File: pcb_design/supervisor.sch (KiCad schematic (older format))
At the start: 27 parts

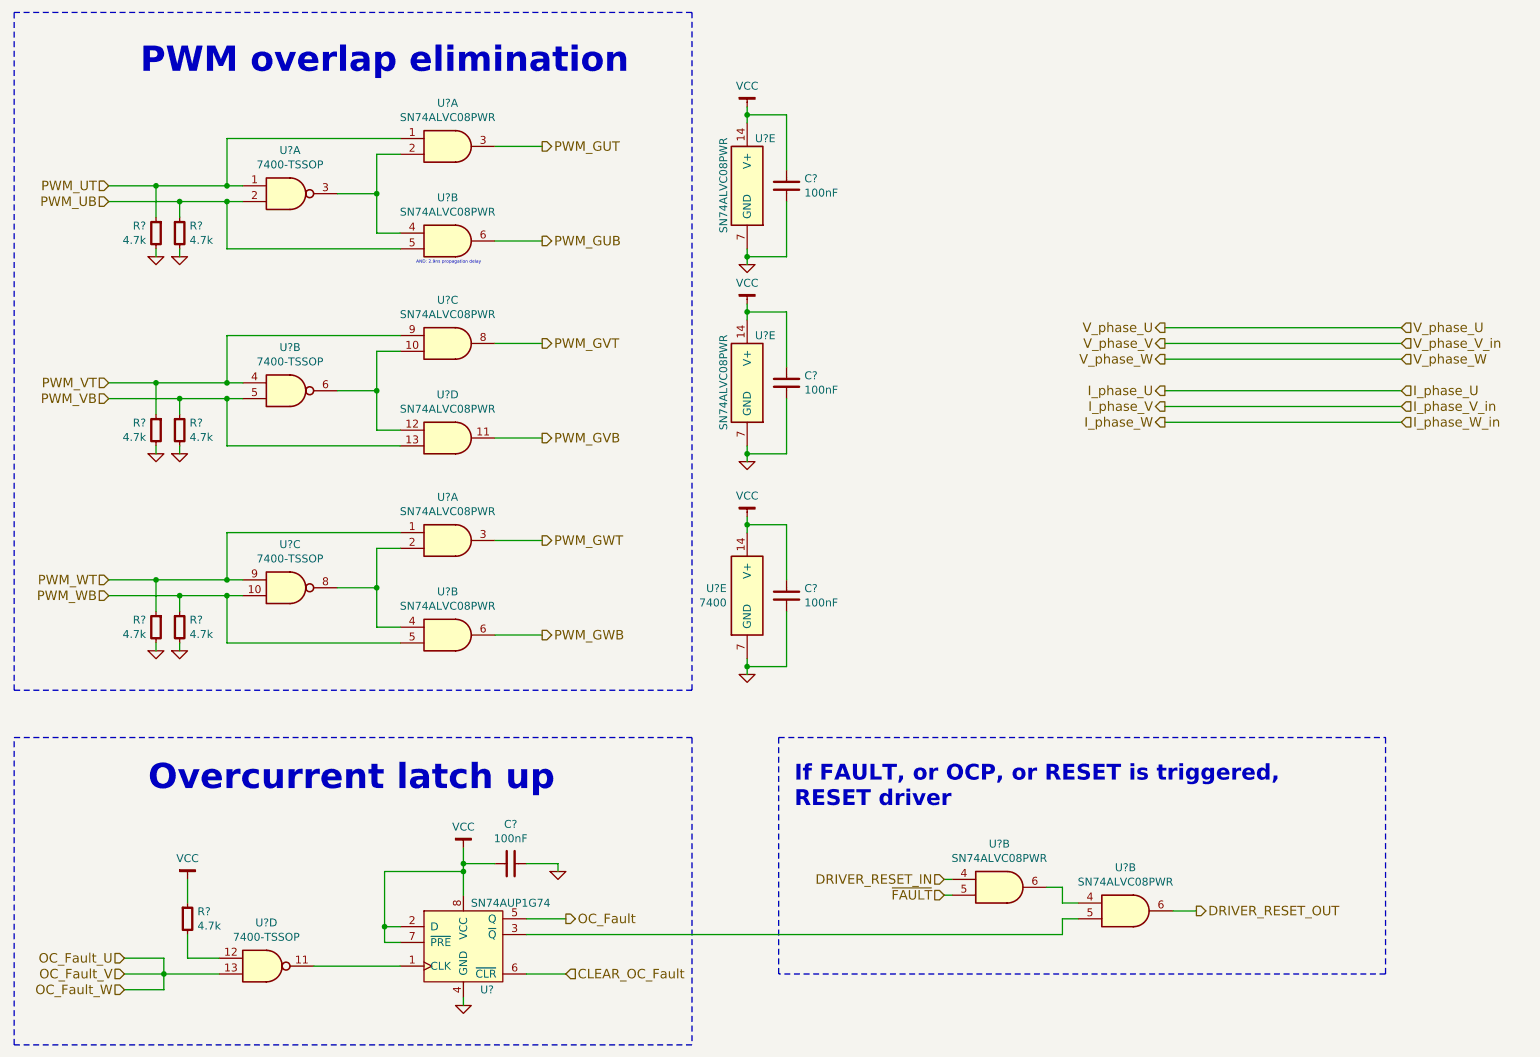
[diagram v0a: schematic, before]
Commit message: Updated MCU sheet to comply with VESC 6 pinout. Added 5v analog inputs and updated some labels
Signed-off-by: Marcos Chaparro <mchaparro@paltatech.com>
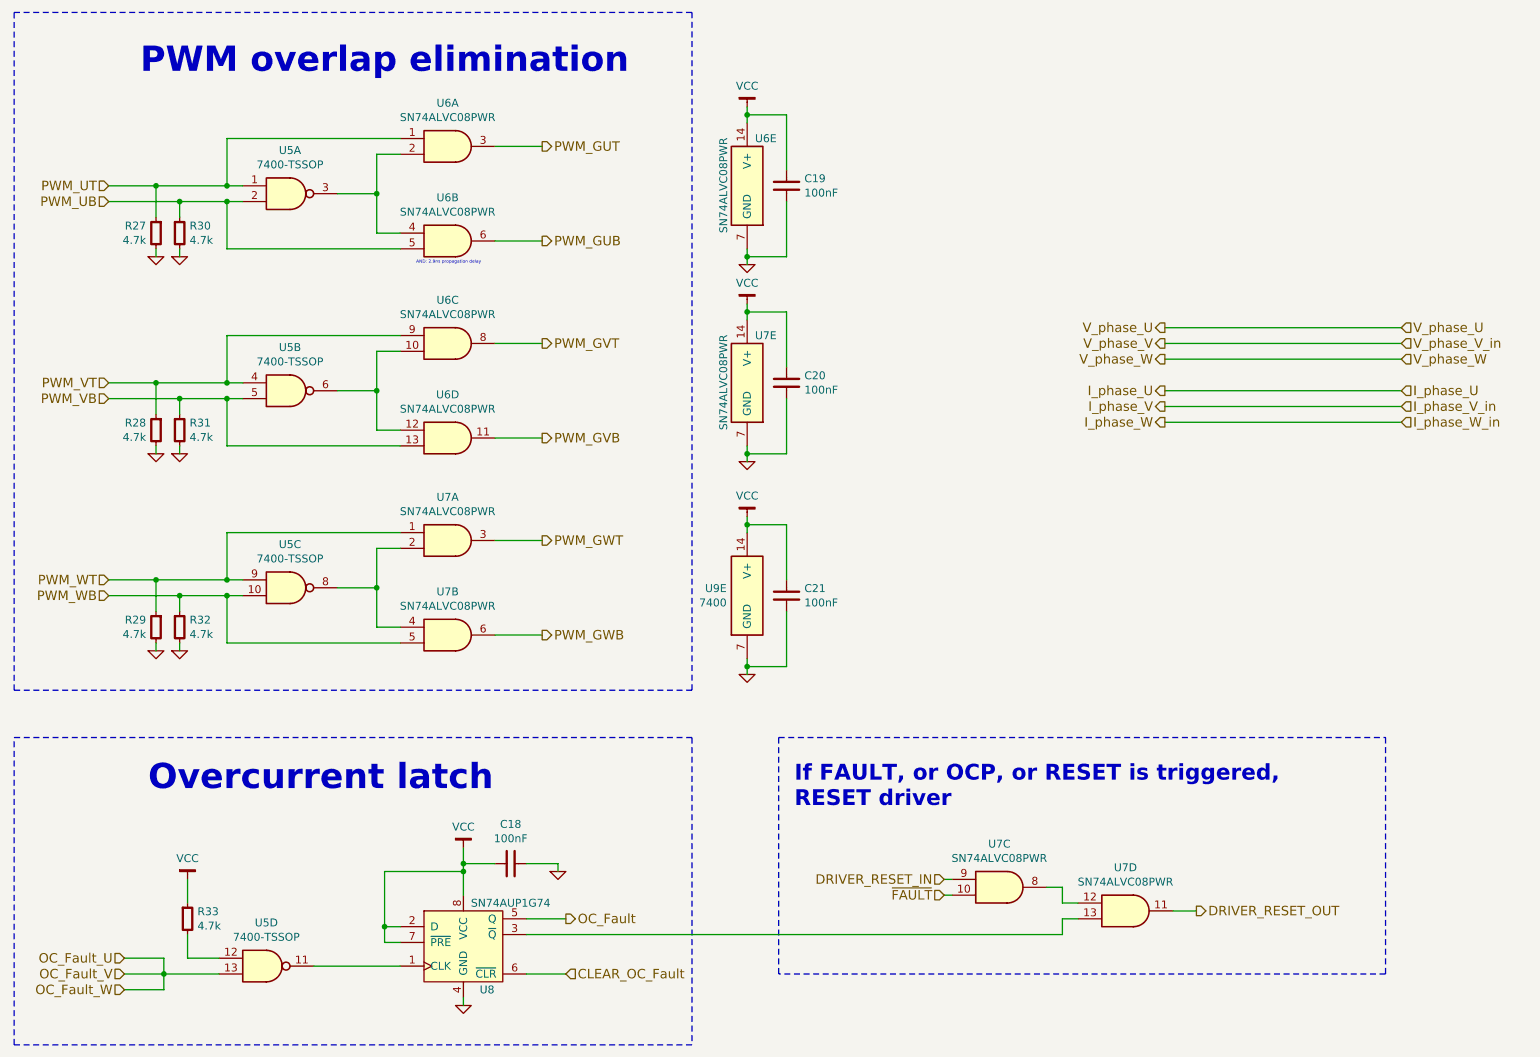
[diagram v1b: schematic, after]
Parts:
- gave numbers to parts that had none: 16
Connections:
- net DRIVER_RESET_IN: now also U7.9 (D1C); no longer U7.4 (D1B)
- net DRIVER_RESET_OUT: now also U7.11 (QD); no longer U7.6 (QB)
- net ~FAULT: now also U7.10 (D2C); no longer U7.5 (D2B)
- net at U8.3 (~Q): now also U7.13 (D2D); no longer U7.5 (D2B)
- new net: U7.12 (D1D), U7.8 (QC)
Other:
- note added: "Overcurrent latch"
- note removed: "Overcurrent latch up"

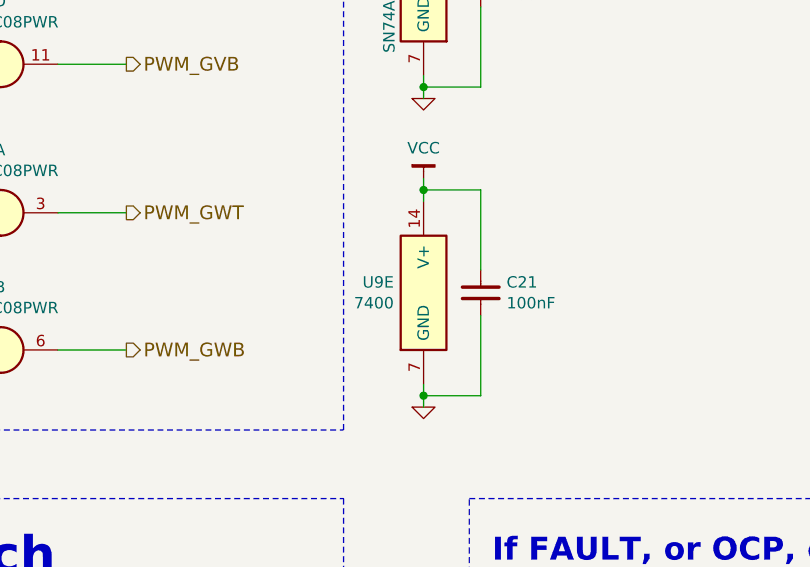
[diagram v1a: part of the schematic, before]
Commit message: Components placement, 3D models, updated some footprints to nominal IPC type
Signed-off-by: Marcos Chaparro <mchaparro@paltatech.com>
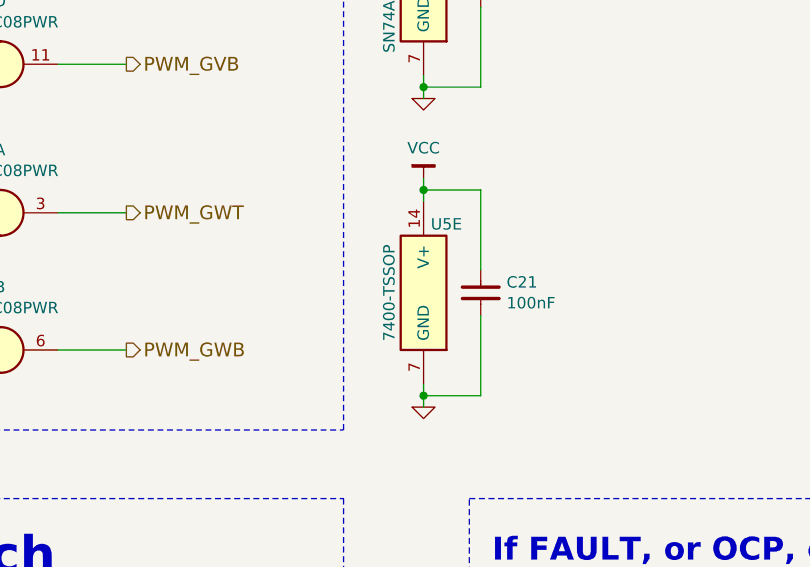
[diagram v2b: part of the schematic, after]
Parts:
- removed U9: 7400, symbol 7400
- added unit 5 of U5
- U8: footprint (none) -> IPC7351-Nominal:SOP50P310X100-8
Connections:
- net GND: now also U5.7 (GND)
- net VCC: now also U5.14 (V+)
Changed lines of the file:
@@
 $Descr A4 11693 8268
 encoding utf-8
-Sheet 8 12
+Sheet 7 12
 Title ""
 Date ""
@@
 Connection ~ 2000 2050
 $Comp
-L GND #PWR056
+L GND #PWR44
 U 1 1 588831C2
 P 1850 2400
-F 0 "#PWR056" H 1850 2400 30  0001 C CNN
+F 0 "#PWR44" H 1850 2400 30  0001 C CNN
 F 1 "GND" H 1850 2330 30  0001 C CNN
 F 2 "" H 1850 2400 60  0000 C CNN
@@
 	1850 2400 1850 2350
 $Comp
-L GND #PWR057
+L GND #PWR47
 U 1 1 58883201
 P 2000 2400
-F 0 "#PWR057" H 2000 2400 30  0001 C CNN
+F 0 "#PWR47" H 2000 2400 30  0001 C CNN
 F 1 "GND" H 2000 2330 30  0001 C CNN
 F 2 "" H 2000 2400 60  0000 C CNN
@@
 	1    2700 2000
 	1    0    0    -1
-$EndComp
-$Comp
-L 7400 U9
-U 5 1 588843C8
-P 5600 4150
-F 0 "U9" H 5730 3796 50  0000 L CNN
-F 1 "7400" H 5730 3705 50  0000 L CNN
-F 2 "" H 5600 3250 50  0001 C CNN
-F 3 "http://www.nxp.com/documents/data_sheet/74HC_HCT00.pdf" H 5600 3150 50  0001 C CNN
-	5    5600 4150
-	-1   0    0    -1
 $EndComp
 $Comp
@@
 Connection ~ 2000 3300
 $Comp
-L GND #PWR058
+L GND #PWR45
 U 1 1 588824FD
 P 1850 3650
-F 0 "#PWR058" H 1850 3650 30  0001 C CNN
+F 0 "#PWR45" H 1850 3650 30  0001 C CNN
 F 1 "GND" H 1850 3580 30  0001 C CNN
 F 2 "" H 1850 3650 60  0000 C CNN
@@
 	1850 3650 1850 3600
 $Comp
-L GND #PWR059
+L GND #PWR48
 U 1 1 58882504
 P 2000 3650
-F 0 "#PWR059" H 2000 3650 30  0001 C CNN
+F 0 "#PWR48" H 2000 3650 30  0001 C CNN
 F 1 "GND" H 2000 3580 30  0001 C CNN
 F 2 "" H 2000 3650 60  0000 C CNN
@@
 Connection ~ 2000 4550
 $Comp
-L GND #PWR060
+L GND #PWR46
 U 1 1 5888288C
 P 1850 4900
-F 0 "#PWR060" H 1850 4900 30  0001 C CNN
+F 0 "#PWR46" H 1850 4900 30  0001 C CNN
 F 1 "GND" H 1850 4830 30  0001 C CNN
 F 2 "" H 1850 4900 60  0000 C CNN
@@
 	1850 4900 1850 4850
 $Comp
-L GND #PWR061
+L GND #PWR49
 U 1 1 58882893
 P 2000 4900
-F 0 "#PWR061" H 2000 4900 30  0001 C CNN
+F 0 "#PWR49" H 2000 4900 30  0001 C CNN
 F 1 "GND" H 2000 4830 30  0001 C CNN
 F 2 "" H 2000 4900 60  0000 C CNN
@@
 F 0 "U8" H 3950 6550 50  0000 C CNN
 F 1 "SN74AUP1G74" H 4100 7100 50  0000 C CNN
-F 2 "" H 3800 6800 20  0001 C CNN
+F 2 "IPC7351-Nominal:SOP50P310X100-8" H 3800 6800 20  0001 C CNN
 F 3 "" H 3800 6800 20  0001 C CNN
 	1    3800 6800
@@
 $EndComp
 $Comp
-L GND #PWR062
+L GND #PWR52
 U 1 1 5888A11E
 P 3800 7150
-F 0 "#PWR062" H 3800 7150 30  0001 C CNN
+F 0 "#PWR52" H 3800 7150 30  0001 C CNN
 F 1 "GND" H 3800 7080 30  0001 C CNN
 F 2 "" H 3800 7150 60  0000 C CNN
@@
 	4400 6250 4400 6300
 $Comp
-L GND #PWR063
+L GND #PWR53
 U 1 1 5888A46C
 P 4400 6300
-F 0 "#PWR063" H 4400 6300 30  0001 C CNN
+F 0 "#PWR53" H 4400 6300 30  0001 C CNN
 F 1 "GND" H 4400 6230 30  0001 C CNN
 F 2 "" H 4400 6300 60  0000 C CNN
@@
 AR Path="/5886DA84/588980B5" Ref="#PWR?"  Part="1"
 AR Path="/588C2790/588980B5" Ref="#PWR?"  Part="1"
-AR Path="/5888D059/588980B5" Ref="#PWR064"  Part="1"
-F 0 "#PWR064" H 3800 6200 30  0001 C CNN
+AR Path="/5888D059/588980B5" Ref="#PWR51"  Part="1"
+F 0 "#PWR51" H 3800 6200 30  0001 C CNN
 F 1 "VCC" H 3800 6283 50  0000 C CNN
 F 2 "" H 3800 6150 60  0000 C CNN
@@
 AR Path="/5886DA84/58898103" Ref="#PWR?"  Part="1"
 AR Path="/588C2790/58898103" Ref="#PWR?"  Part="1"
-AR Path="/5888D059/58898103" Ref="#PWR065"  Part="1"
-F 0 "#PWR065" H 2050 6400 30  0001 C CNN
+AR Path="/5888D059/58898103" Ref="#PWR50"  Part="1"
+F 0 "#PWR50" H 2050 6400 30  0001 C CNN
 F 1 "VCC" H 2050 6483 50  0000 C CNN
 F 2 "" H 2050 6350 60  0000 C CNN
@@
 AR Path="/5886DA84/588981CE" Ref="#PWR?"  Part="1"
 AR Path="/588C2790/588981CE" Ref="#PWR?"  Part="1"
-AR Path="/5888D059/588981CE" Ref="#PWR066"  Part="1"
-F 0 "#PWR066" H 5600 4100 30  0001 C CNN
+AR Path="/5888D059/588981CE" Ref="#PWR58"  Part="1"
+F 0 "#PWR58" H 5600 4100 30  0001 C CNN
 F 1 "VCC" H 5600 4183 50  0000 C CNN
 F 2 "" H 5600 4050 60  0000 C CNN
@@
 AR Path="/5886DA84/58898412" Ref="#PWR?"  Part="1"
 AR Path="/588C2790/58898412" Ref="#PWR?"  Part="1"
-AR Path="/5888D059/58898412" Ref="#PWR067"  Part="1"
-F 0 "#PWR067" H 5600 1500 30  0001 C CNN
+AR Path="/5888D059/58898412" Ref="#PWR54"  Part="1"
+F 0 "#PWR54" H 5600 1500 30  0001 C CNN
 F 1 "VCC" H 5600 1583 50  0000 C CNN
 F 2 "" H 5600 1450 60  0000 C CNN
@@
 AR Path="/5886DA84/588984F1" Ref="#PWR?"  Part="1"
 AR Path="/588C2790/588984F1" Ref="#PWR?"  Part="1"
-AR Path="/5888D059/588984F1" Ref="#PWR068"  Part="1"
-F 0 "#PWR068" H 5600 2750 30  0001 C CNN
+AR Path="/5888D059/588984F1" Ref="#PWR56"  Part="1"
+F 0 "#PWR56" H 5600 2750 30  0001 C CNN
 F 1 "VCC" H 5600 2833 50  0000 C CNN
 F 2 "" H 5600 2700 60  0000 C CNN
@@
 	5600 4950 5600 5050
 $Comp
-L GND #PWR069
+L GND #PWR59
 U 1 1 58899228
 P 5600 5050
-F 0 "#PWR069" H 5600 5050 30  0001 C CNN
+F 0 "#PWR59" H 5600 5050 30  0001 C CNN
 F 1 "GND" H 5600 4980 30  0001 C CNN
 F 2 "" H 5600 5050 60  0000 C CNN
@@
 Connection ~ 5600 5000
 $Comp
-L GND #PWR070
+L GND #PWR57
 U 1 1 5889937C
 P 5600 3700
-F 0 "#PWR070" H 5600 3700 30  0001 C CNN
+F 0 "#PWR57" H 5600 3700 30  0001 C CNN
 F 1 "GND" H 5600 3630 30  0001 C CNN
 F 2 "" H 5600 3700 60  0000 C CNN
@@
 $EndComp
 $Comp
-L GND #PWR071
+L GND #PWR55
 U 1 1 588993D2
 P 5600 2450
-F 0 "#PWR071" H 5600 2450 30  0001 C CNN
+F 0 "#PWR55" H 5600 2450 30  0001 C CNN
 F 1 "GND" H 5600 2380 30  0001 C CNN
 F 2 "" H 5600 2450 60  0000 C CNN
@@
 	5850 1500 5600 1500
 Connection ~ 5600 1500
+$Comp
+L 7400 U5
+U 5 1 588A2A9D
+P 5600 4150
+F 0 "U5" H 5700 4050 50  0000 C CNN
+F 1 "7400-TSSOP" V 5450 3750 50  0000 C CNN
+F 2 "IPC7351-Nominal:SOP65P640X110-14" H 5600 3250 50  0001 C CNN
+F 3 "http://www.nxp.com/documents/data_sheet/74HC_HCT00.pdf" H 5600 3150 50  0001 C CNN
+	5    5600 4150
+	1    0    0    -1
+$EndComp
 $EndSCHEMATC
